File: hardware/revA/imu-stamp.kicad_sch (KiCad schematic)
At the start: 18 parts, among them P1 I/O, P2 I/O, U1 LTC4317, U2 REG710NA-3.3/3K

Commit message: consistency updates
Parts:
- removed R1, R5: 10k, Resistor_SMD:R_0201_0603Metric, symbol Device:R_US
- R2: value 845k -> ~; footprint (none) -> Resistor_SMD:R_0402_1005Metric; now not fitted; now in the parts list
- R3: value 61.9k -> ~; footprint (none) -> Resistor_SMD:R_0402_1005Metric; now not fitted; now in the parts list
- R4: value 93.1k -> ~; footprint (none) -> Resistor_SMD:R_0402_1005Metric; now not fitted; now in the parts list
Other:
- note added: "For proto/breadboard use without a PCB to set address."
- note added: "I2C ADDRESS SELECT REAR"
- note removed: "I2C ADDRESS SELECT EXAMPLE"
- note removed: "XOR1 = 0x2 XOR2 = 0x4"

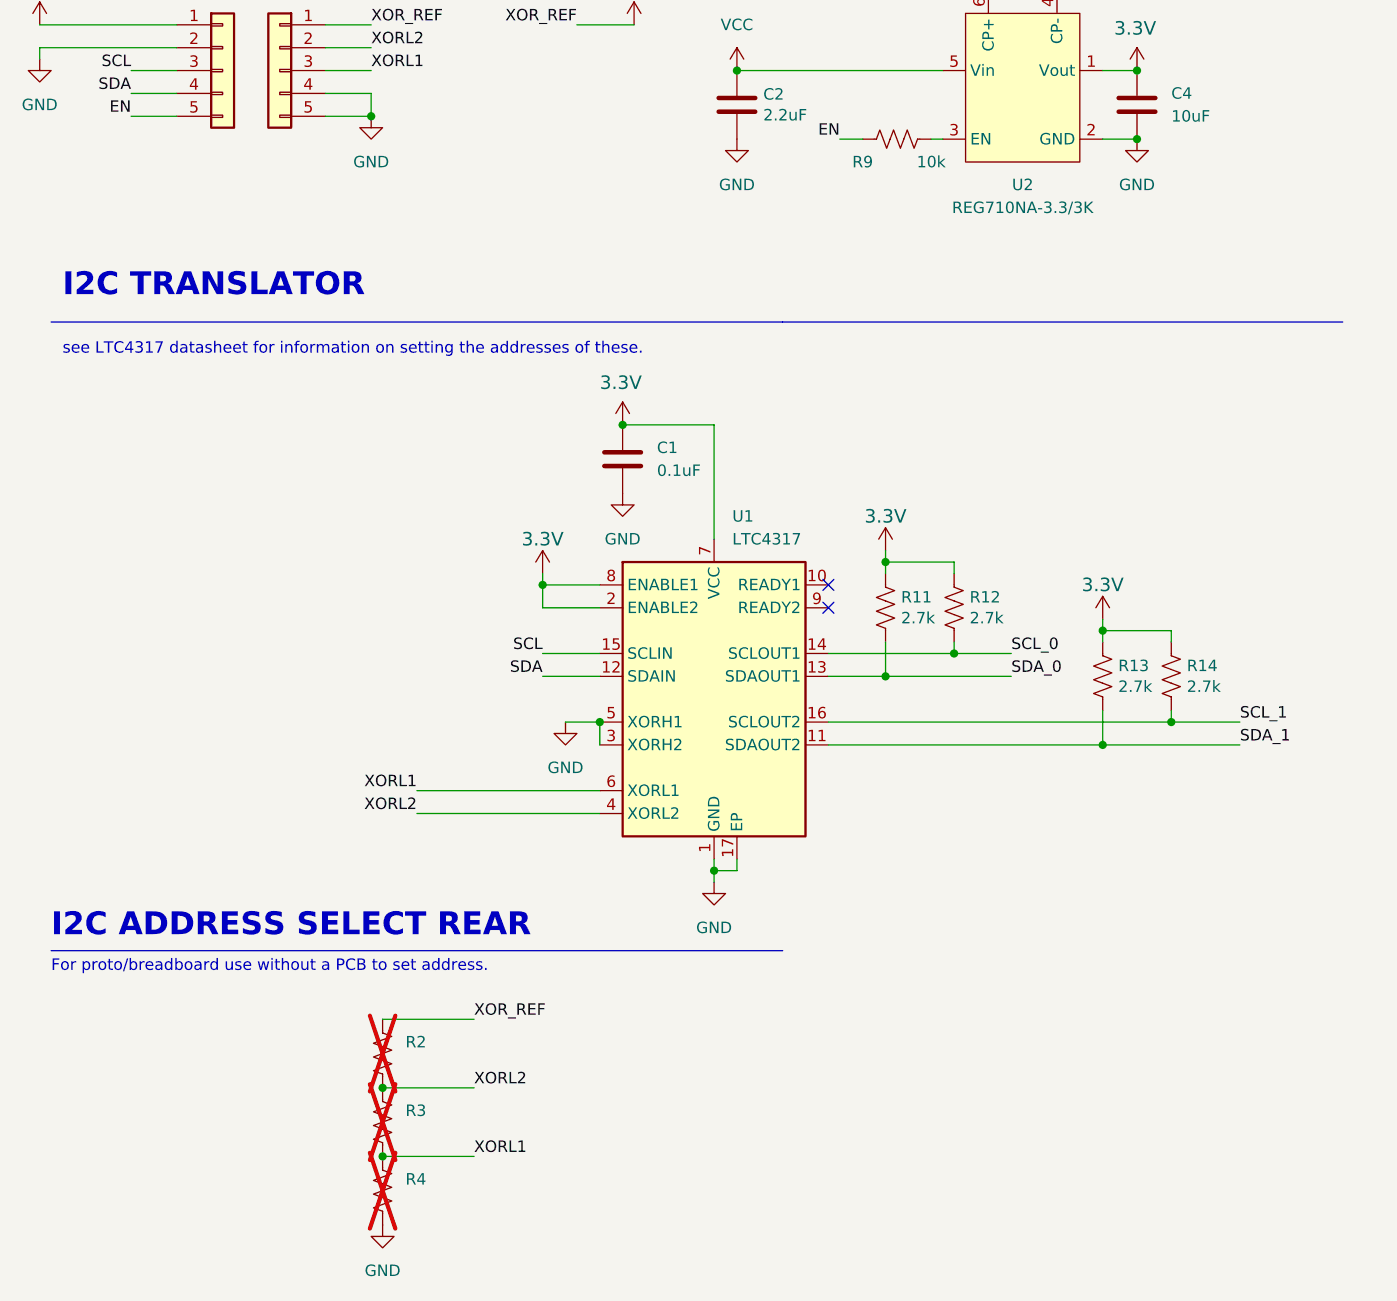
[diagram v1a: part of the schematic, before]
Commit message: resized board for manufacturing
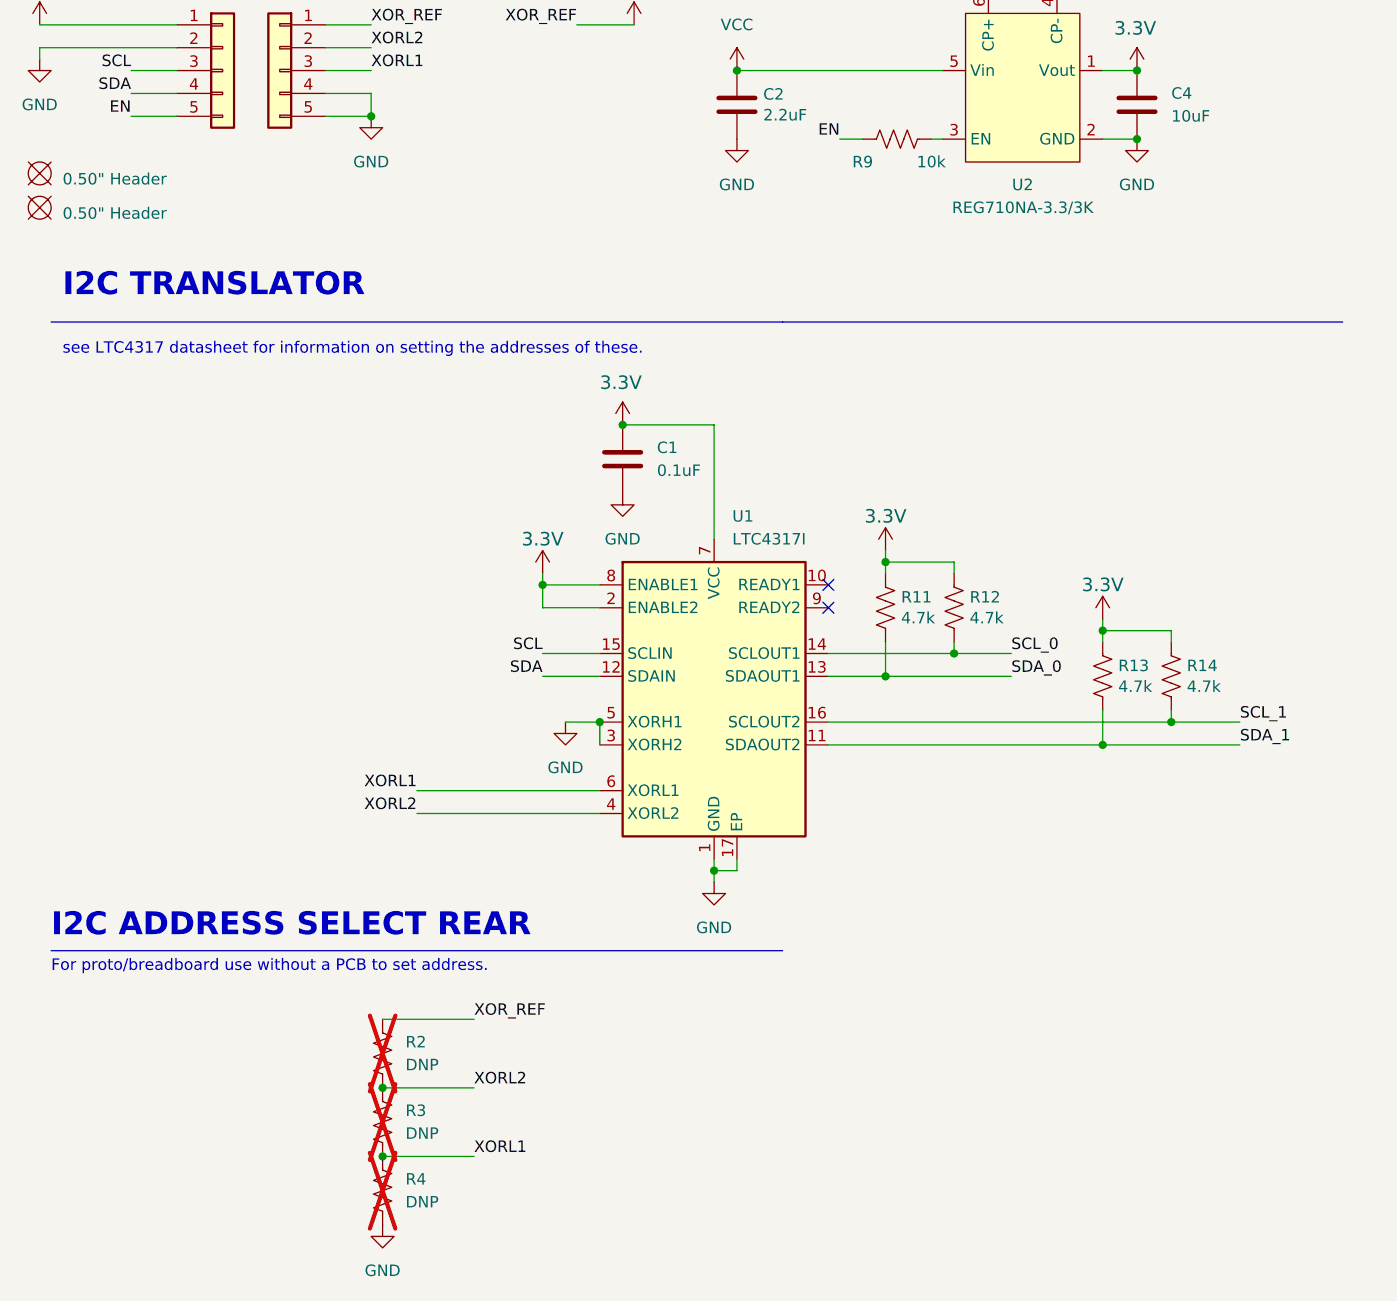
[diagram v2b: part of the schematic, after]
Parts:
- added BOM1, BOM2: 0.50" Header, symbol SierraLobo:BOMTIE
- C4: footprint Capacitor_SMD:C_0402_1005Metric -> Capacitor_SMD:C_0603_1608Metric
- P1, P2: footprint imu-stamp:PinHeaderCastellated_1x05_P1.27mm_Vertical -> imu-stamp:Castellated_1x05_P1.27mm_Vertical
- R11, R12, R13, R14: value 2.7k -> 4.7k
- R2, R3, R4: value ~ -> DNP
- U1: value LTC4317 -> LTC4317I
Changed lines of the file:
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@@
       (effects (font (size 1.27 1.27)) (justify left))
     )
-    (property "Footprint" "Capacitor_SMD:C_0402_1005Metric" (at 139.3952 67.31 0)
+    (property "Footprint" "Capacitor_SMD:C_0603_1608Metric" (at 139.3952 67.31 0)
       (effects (font (size 1.27 1.27)) hide)
     )
@@
       (effects (font (size 1.27 1.27)) hide)
     )
-    (property "Footprint" "imu-stamp:PinHeaderCastellated_1x05_P1.27mm_Vertical" (at 43.18 59.69 0)
+    (property "Footprint" "imu-stamp:Castellated_1x05_P1.27mm_Vertical" (at 43.18 59.69 0)
       (effects (font (size 1.27 1.27)) hide)
     )
@@
       (effects (font (size 1.27 1.27)) hide)
     )
-    (property "Footprint" "imu-stamp:PinHeaderCastellated_1x05_P1.27mm_Vertical" (at 36.83 59.69 0)
+    (property "Footprint" "imu-stamp:Castellated_1x05_P1.27mm_Vertical" (at 36.83 59.69 0)
       (effects (font (size 1.27 1.27)) hide)
     )
@@
       (effects (font (size 1.27 1.27)) (justify left))
     )
-    (property "Value" "2.7k" (at 136.3472 128.143 0)
+    (property "Value" "4.7k" (at 136.3472 128.143 0)
       (effects (font (size 1.27 1.27)) (justify left))
     )
@@
       (effects (font (size 1.27 1.27)) (justify left))
     )
-    (property "Value" "~" (at 57.15 185.4199 0)
+    (property "Value" "DNP" (at 57.15 185.4199 0)
       (effects (font (size 1.27 1.27)) (justify left))
     )
@@
       (effects (font (size 1.27 1.27)) (justify left))
     )
-    (property "Value" "LTC4317" (at 93.4594 111.76 0)
+    (property "Value" "LTC4317I" (at 93.4594 111.76 0)
       (effects (font (size 1.27 1.27)) (justify left))
     )
@@
       (effects (font (size 1.27 1.27)) hide)
     )
-    (property "Datasheet" "LTC4317CDHC#PBF" (at 76.2 87.63 0)
+    (property "Datasheet" "LTC4317IDHC" (at 76.2 87.63 0)
       (effects (font (size 1.27 1.27)) hide)
     )
@@
       (effects (font (size 1.27 1.27)) (justify left))
     )
-    (property "Value" "2.7k" (at 143.9672 128.143 0)
+    (property "Value" "4.7k" (at 143.9672 128.143 0)
       (effects (font (size 1.27 1.27)) (justify left))
     )
@@
       (effects (font (size 1.27 1.27)) (justify left))
     )
-    (property "Value" "2.7k" (at 119.8372 120.523 0)
+    (property "Value" "4.7k" (at 119.8372 120.523 0)
       (effects (font (size 1.27 1.27)) (justify left))
     )
@@
         (path "/5c93d476-08a7-4304-b21e-98f5ca275563"
           (reference "R12") (unit 1)
+        )
+      )
+    )
+  )
+  (symbol (lib_id "SierraLobo:BOMTIE") (at 16.51 71.12 0) (unit 1)
+    (in_bom yes) (on_board no) (dnp no) (fields_autoplaced)
+    (property "Reference" "BOM1" (at 16.51 68.58 0)
+      (effects (font (size 1.27 1.27)) hide)
+    )
+    (property "Value" "0.50\" Header" (at 19.05 71.755 0)
+      (effects (font (size 1.27 1.27)) (justify left))
+    )
+    (property "Footprint" "" (at 16.51 71.12 0)
+      (effects (font (size 1.27 1.27)) hide)
+    )
+    (property "Datasheet" "M50-3530542" (at 16.51 71.12 0)
+      (effects (font (size 1.27 1.27)) hide)
+    )
+    (property "Sim.Enable" "0" (at 16.51 71.12 0)
+      (effects (font (size 1.27 1.27)) hide)
+    )
+    (instances
+      (project "imu-stamp"
+        (path "/5c93d476-08a7-4304-b21e-98f5ca275563"
+          (reference "BOM1") (unit 1)
         )
       )
@@
       (effects (font (size 1.27 1.27)) (justify left))
     )
-    (property "Value" "~" (at 57.15 177.7999 0)
+    (property "Value" "DNP" (at 57.15 177.7999 0)
       (effects (font (size 1.27 1.27)) (justify left))
     )
@@
       (effects (font (size 1.27 1.27)) (justify left))
     )
-    (property "Value" "~" (at 57.15 170.1799 0)
+    (property "Value" "DNP" (at 57.15 170.1799 0)
       (effects (font (size 1.27 1.27)) (justify left))
     )
@@
         (path "/5c93d476-08a7-4304-b21e-98f5ca275563"
           (reference "C2") (unit 1)
+        )
+      )
+    )
+  )
+  (symbol (lib_id "SierraLobo:BOMTIE") (at 16.51 74.93 0) (unit 1)
+    (in_bom yes) (on_board no) (dnp no) (fields_autoplaced)
+    (property "Reference" "BOM2" (at 16.51 72.39 0)
+      (effects (font (size 1.27 1.27)) hide)
+    )
+    (property "Value" "0.50\" Header" (at 19.05 75.565 0)
+      (effects (font (size 1.27 1.27)) (justify left))
+    )
+    (property "Footprint" "" (at 16.51 74.93 0)
+      (effects (font (size 1.27 1.27)) hide)
+    )
+    (property "Datasheet" "M50-3530542" (at 16.51 74.93 0)
+      (effects (font (size 1.27 1.27)) hide)
+    )
+    (property "Sim.Enable" "0" (at 16.51 74.93 0)
+      (effects (font (size 1.27 1.27)) hide)
+    )
+    (instances
+      (project "imu-stamp"
+        (path "/5c93d476-08a7-4304-b21e-98f5ca275563"
+          (reference "BOM2") (unit 1)
         )
       )
@@
       (effects (font (size 1.27 1.27)) (justify left))
     )
-    (property "Value" "2.7k" (at 112.2172 120.523 0)
-      (effects (font (size 1.27 1.27)) (justify left))
-    )
+    (property "Value" "4.7k" (at 112.2172 120.523 0)
+      (effects (font (size 1.27 1.27)) (justify left))
+    )

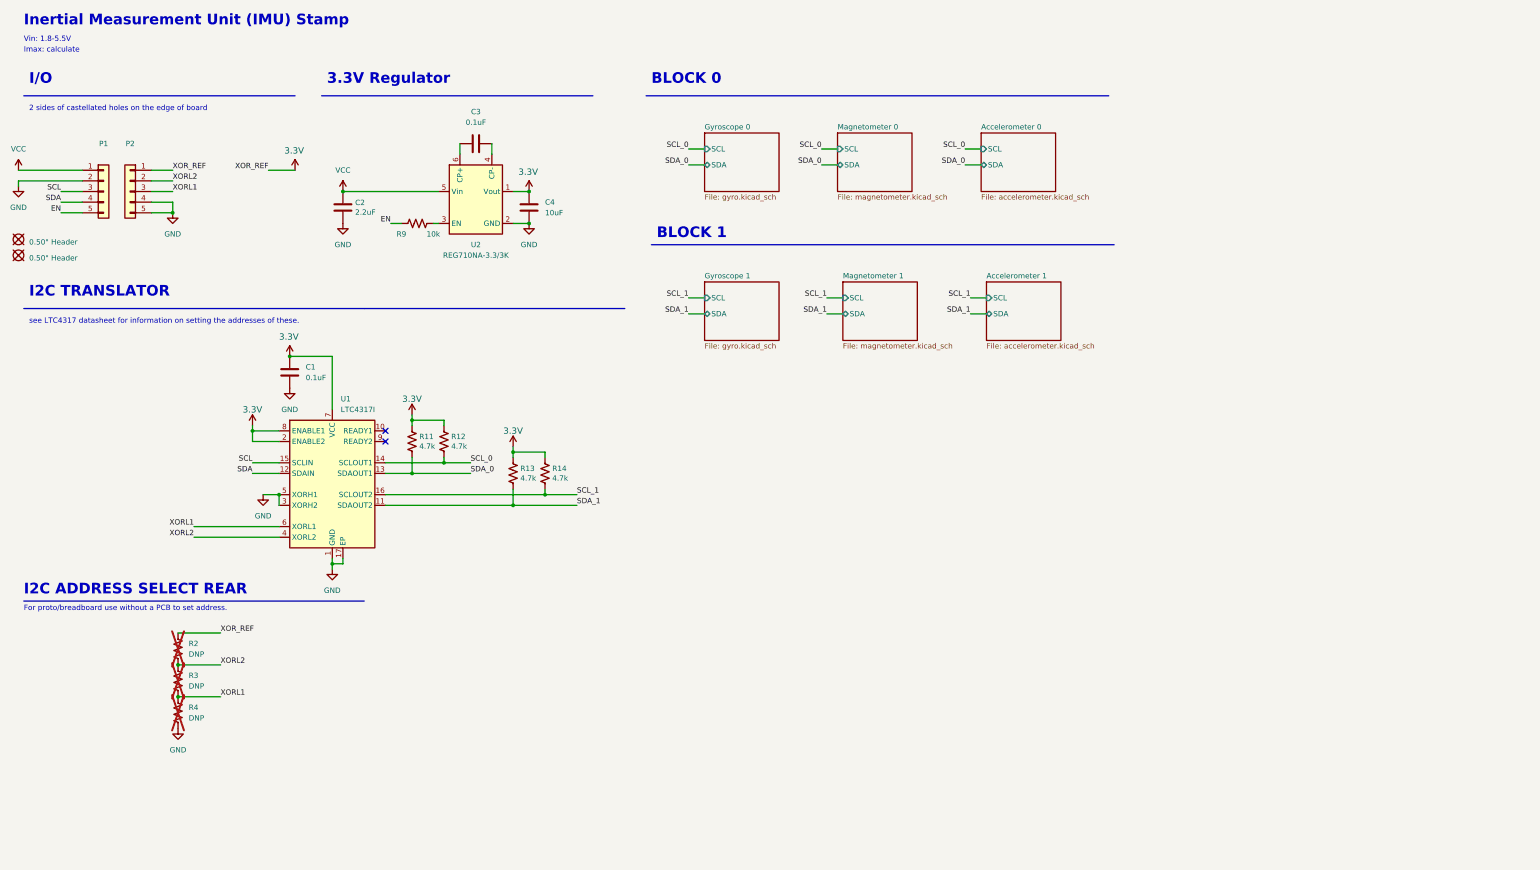
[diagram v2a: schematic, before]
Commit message: added p/n to drawing sheet
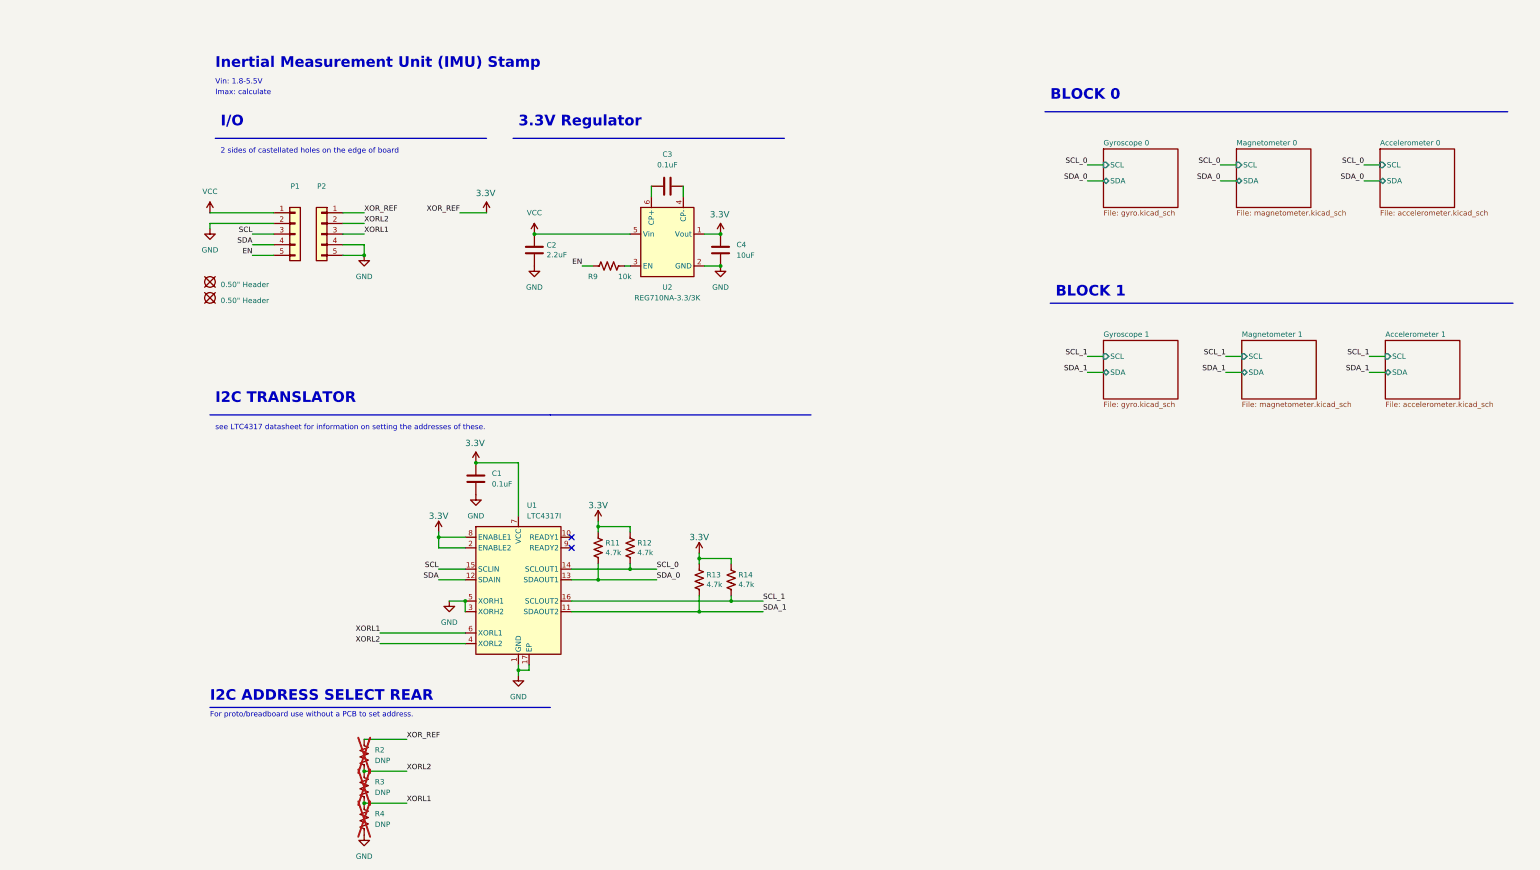
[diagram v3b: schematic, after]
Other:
- title: (none) -> IMU
- moved on the sheet: C1, C2, C3, C4, P1, P2, R11, R12, R13, R14, R2, R3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
